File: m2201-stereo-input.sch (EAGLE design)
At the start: 69 parts, among them U1 ERM1-5MM, U2 ERM1-5MM

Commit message: Add (dummy) FX2 connectors to sch
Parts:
- added U3: FX2-20P-1.27DS, hardware:FX2-20P-1.27DS
- added U4: FX2-20S-1.27DS, hardware:FX2-20S-1.27DS
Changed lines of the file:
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@@
 <part name="GND2" library="supply" deviceset="GND" device=""/>
 <part name="GND5" library="supply" deviceset="GND" device=""/>
+<part name="U3" library="hardware" deviceset="?" device="FX2-20P-1.27DS"/>
+<part name="U4" library="hardware" deviceset="?" device="FX2-20S-1.27DS"/>
 </parts>
 <sheets>
@@
 <instance part="GND2" gate="VR1" x="81.28" y="-43.18"/>
 <instance part="GND5" gate="VR1" x="86.36" y="-43.18"/>
+<instance part="U3" gate="G$1" x="109.22" y="12.7"/>
+<instance part="U4" gate="G$1" x="109.22" y="5.08"/>
 </instances>
 <busses>

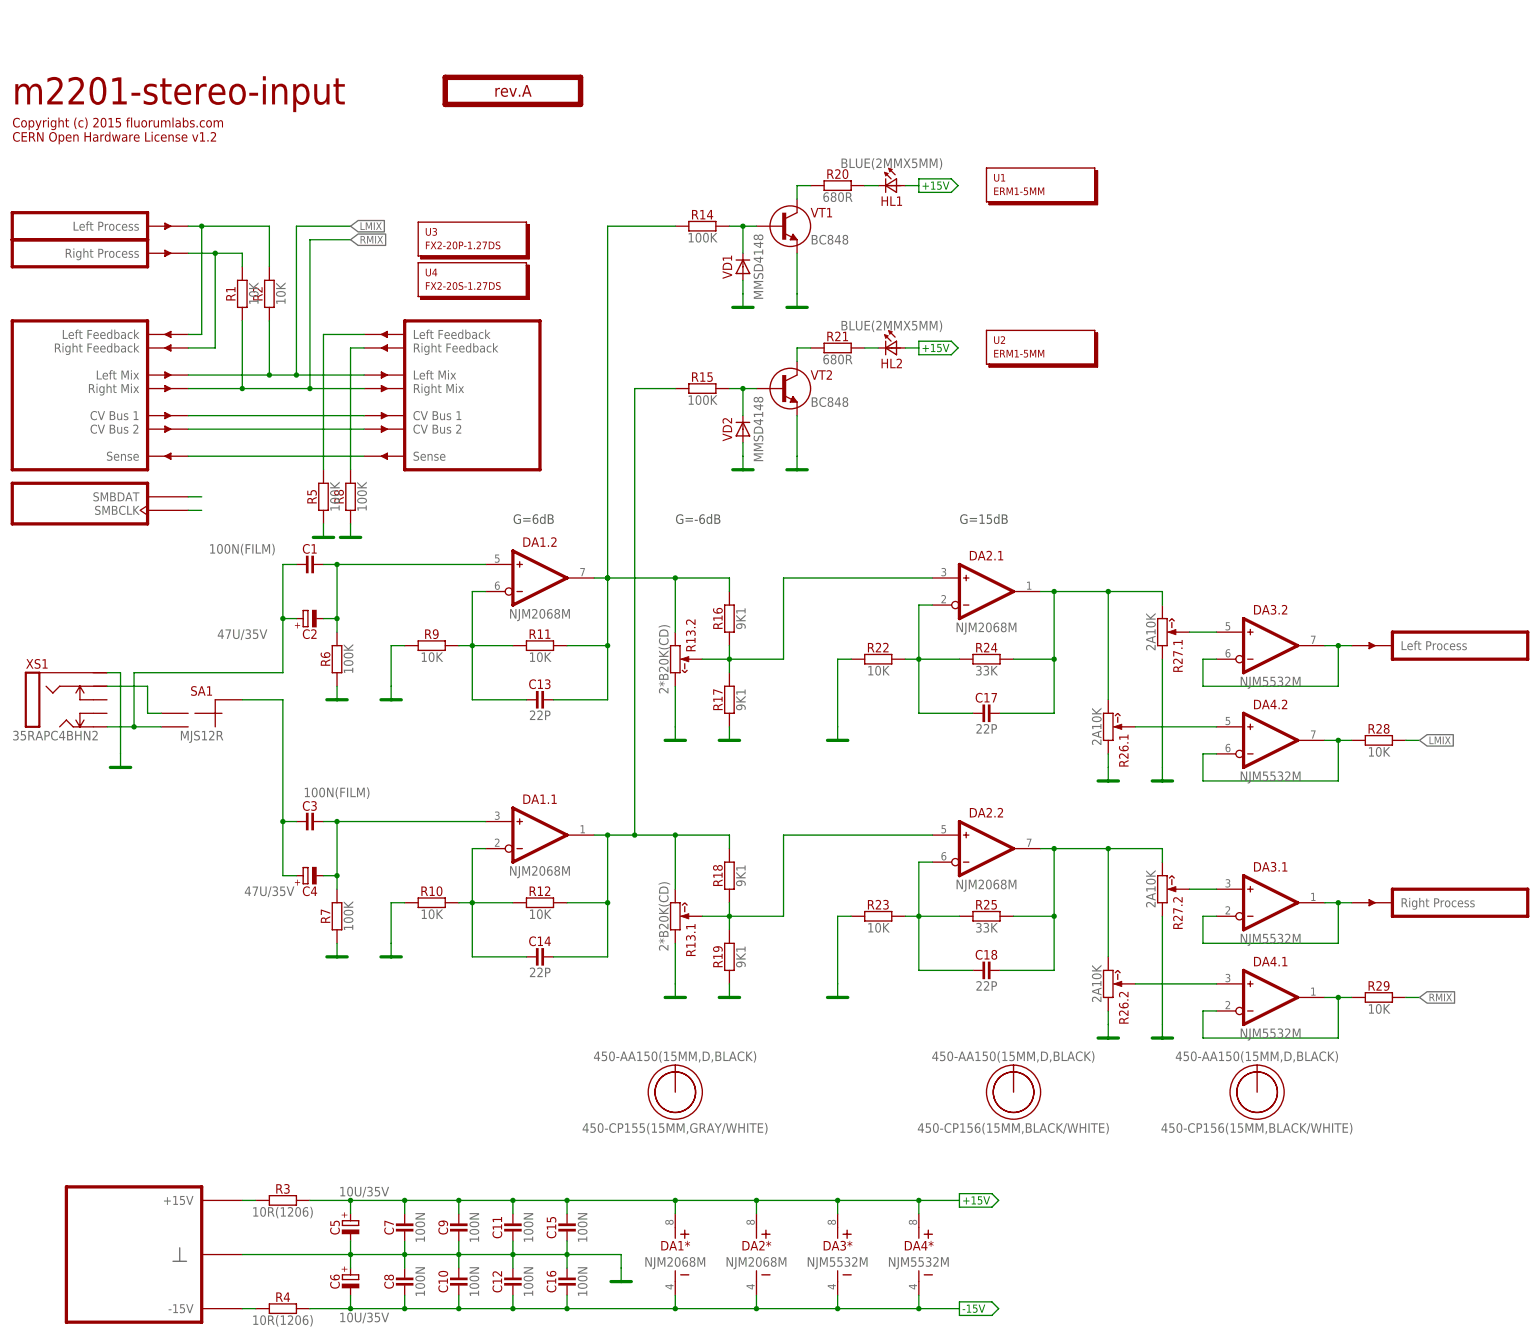
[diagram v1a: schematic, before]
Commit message: Signal indicator refactoring (#5) + no noise when no jack inserted (#6)
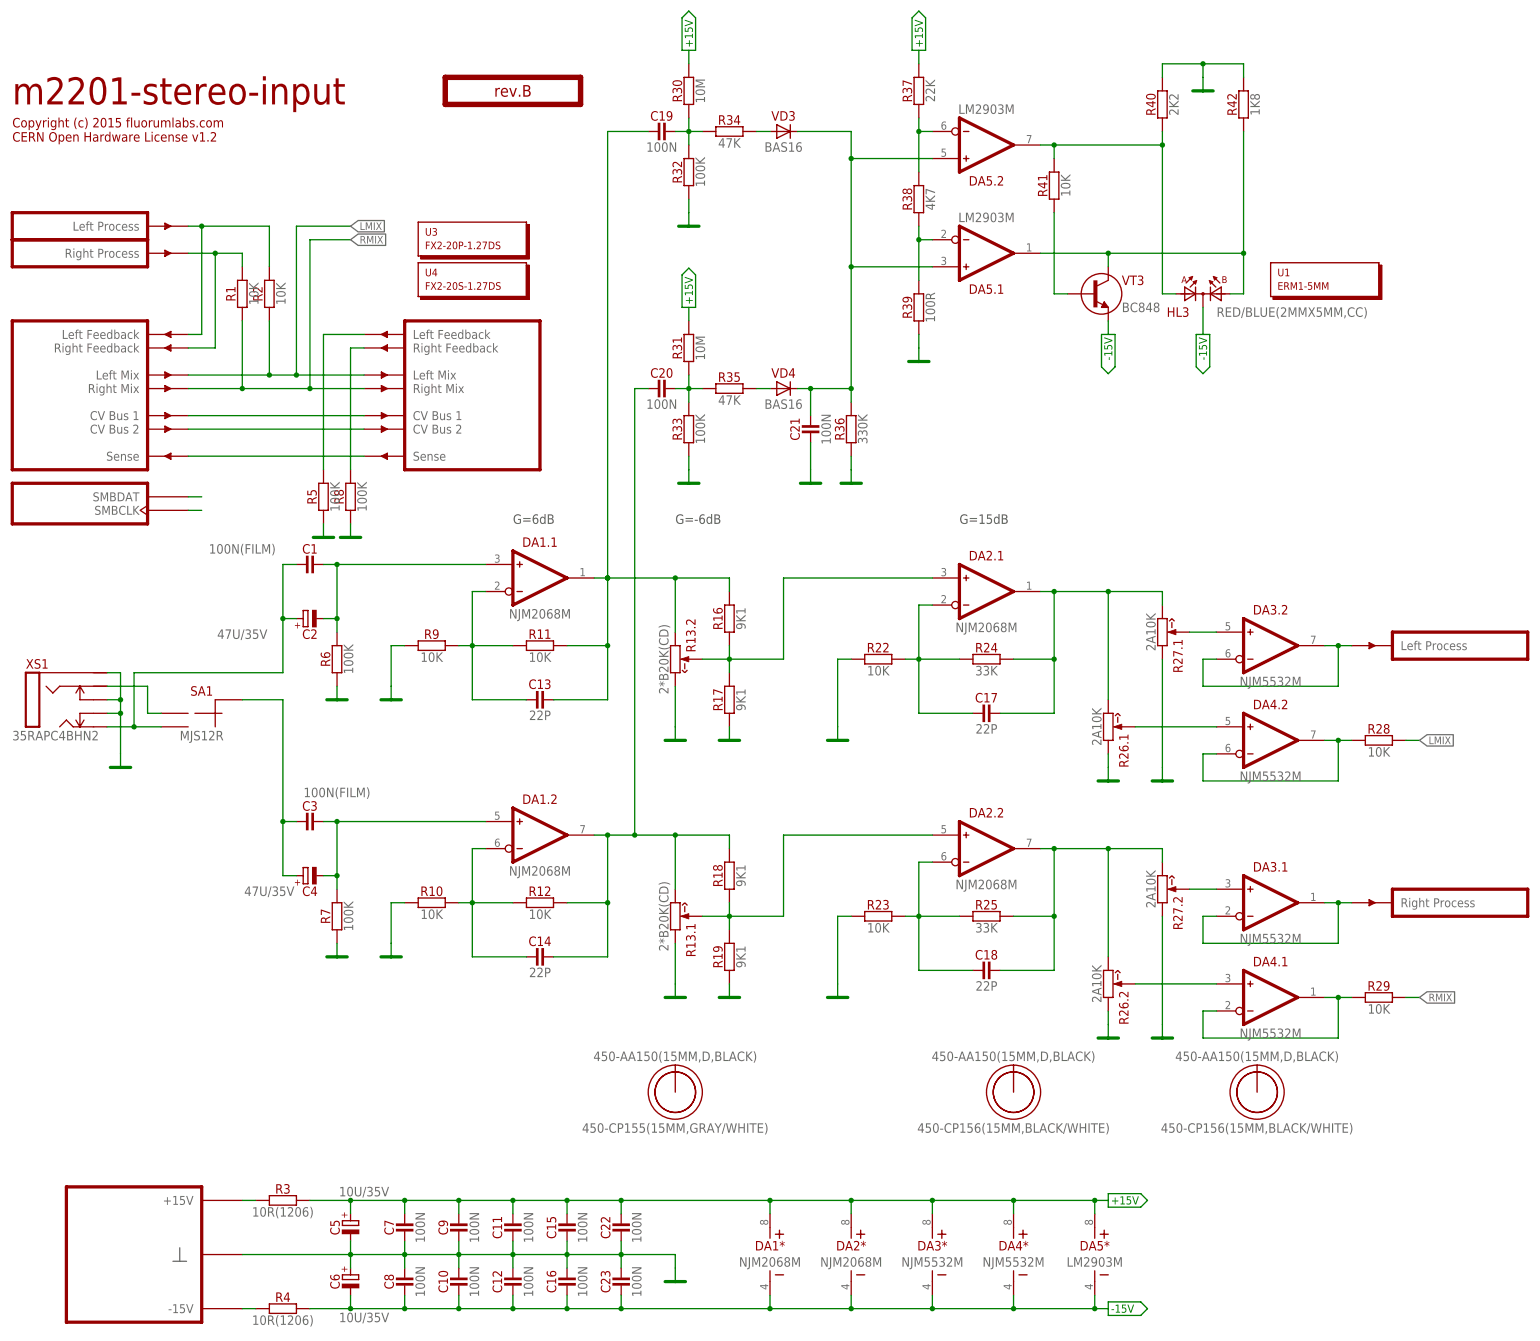
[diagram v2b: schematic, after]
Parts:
- removed HL1, HL2: BLUE(2MMX5MM), optoelectronics:BLUE(2MMX5MM)
- removed R14, R15: 100K, resistors:100K
- removed R20, R21: 680R, resistors:680R
- removed U2: ERM1-5MM, hardware:ERM1-5MM
- removed VD1, VD2: MMSD4148, diodes:MMSD4148
- removed VT1, VT2: BC848, transistors-npn:BC848
- added C19, C20, C21, C22, C23: 100N, capacitors:100N
- added DA5: LM2903M, ic-fairchild:LM2903M
- added HL3: RED/BLUE(2MMX5MM,CC), optoelectronics:RED/BLUE(2MMX5MM,CC)
- added R30, R31: 10M, resistors:10M
- added R32, R33: 100K, resistors:100K
- added R34, R35: 47K, resistors:47K
- added R36: 330K, resistors:330K
- added R37: 22K, resistors:22K
- added R38: 4K7, resistors:4K7
- added R39: 100R, resistors:100R
- added R40: 2K2, resistors:2K2
- added R41: 10K, resistors:10K
- added R42: 1K8, resistors:1K8
- added VD3, VD4: BAS16, diodes:BAS16
- added VT3: BC848, transistors-npn:BC848
- PCB1: value rev.A -> rev.B
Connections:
- removed net N$30: R15.2, VD2.C, VT2.B
- removed net N$32: R21.1, VT2.C
- removed net N$33: HL2.C, R21.2
- removed net N$34: R14.2, VD1.C, VT1.B
- removed net N$35: R20.1, VT1.C
- removed net N$37: HL1.C, R20.2
- new net N$17: C19.2, R30.1, R32.2, R34.1
- new net N$29: R34.2, VD3.A
- new net N$31: C20.2, R31.1, R33.2, R35.1
- new net N$44: R35.2, VD4.A
- new net N$45: C21.2, DA5.1.IN+, DA5.2.IN+, R36.2, VD3.C, VD4.C
- new net N$46: DA5.1.IN-, R38.1, R39.2
- new net N$47: DA5.2.IN-, R37.1, R38.2
- new net N$48: DA5.2.OUT, HL3.A1, R40.1, R41.2
- new net N$49: R41.1, VT3.B
- new net N$51: DA5.1.OUT, HL3.A2, R42.1, VT3.C
- net +15V: now also C22.2, DA5*.V+, R30.2, R31.2, R37.2; no longer HL1.A, HL2.A
- net -15V: now also C23.1, DA5*.V-, HL3.K, VT3.E
- net GND: now also C21.1, C22.1, C23.2, R32.1, R33.1, R36.1, R39.1, R40.2, R42.2, XS1.RN, XS1.TN; no longer VD1.A, VD2.A, VT1.E, VT2.E
- net N$10: now also DA1.1.IN+; no longer DA1.2.IN+
- net N$15: now also C20.1, DA1.2.OUT; no longer DA1.1.OUT, R15.1
- net N$19: now also C19.1, DA1.1.OUT; no longer DA1.2.OUT, R14.1
- net N$26: now also DA1.1.IN-; no longer DA1.2.IN-
- net N$27: now also DA1.2.IN-; no longer DA1.1.IN-
- net N$9: now also DA1.2.IN+; no longer DA1.1.IN+
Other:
- moved on the sheet: DA1*, DA1.1, DA1.2, DA2*, DA3*, DA4*, U1
